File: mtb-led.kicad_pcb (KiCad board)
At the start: 2 copper layers, 120 x 50 mm, 60 parts, among them J7 AVR-ISP-6, J9 DEBUG, SW1 SW_Push, U1 ATmega328PB-A, U2 78M05, U3 TLC5940PWP, U4 TLC5940PWP, U5 MAX487E, Y1 14.7456 MHz

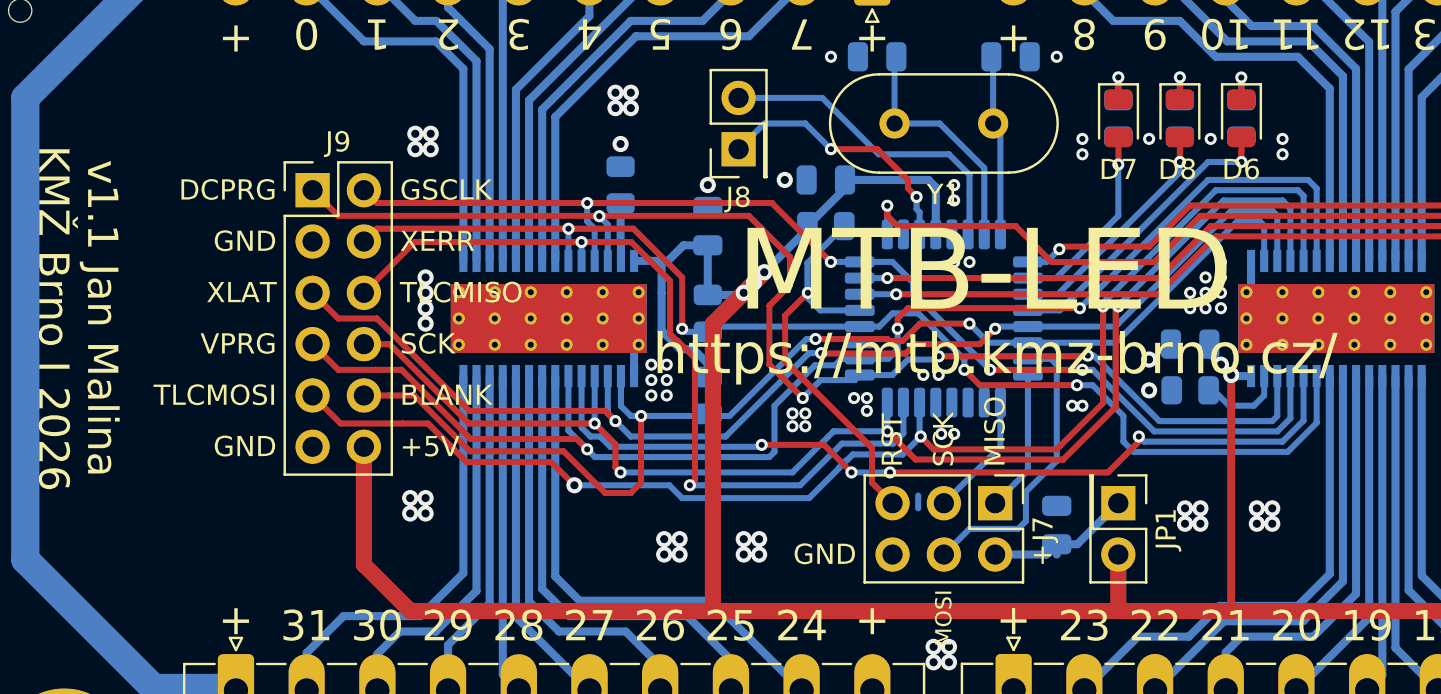
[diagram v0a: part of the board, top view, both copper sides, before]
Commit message: Remove XERR signal.
It is not used.
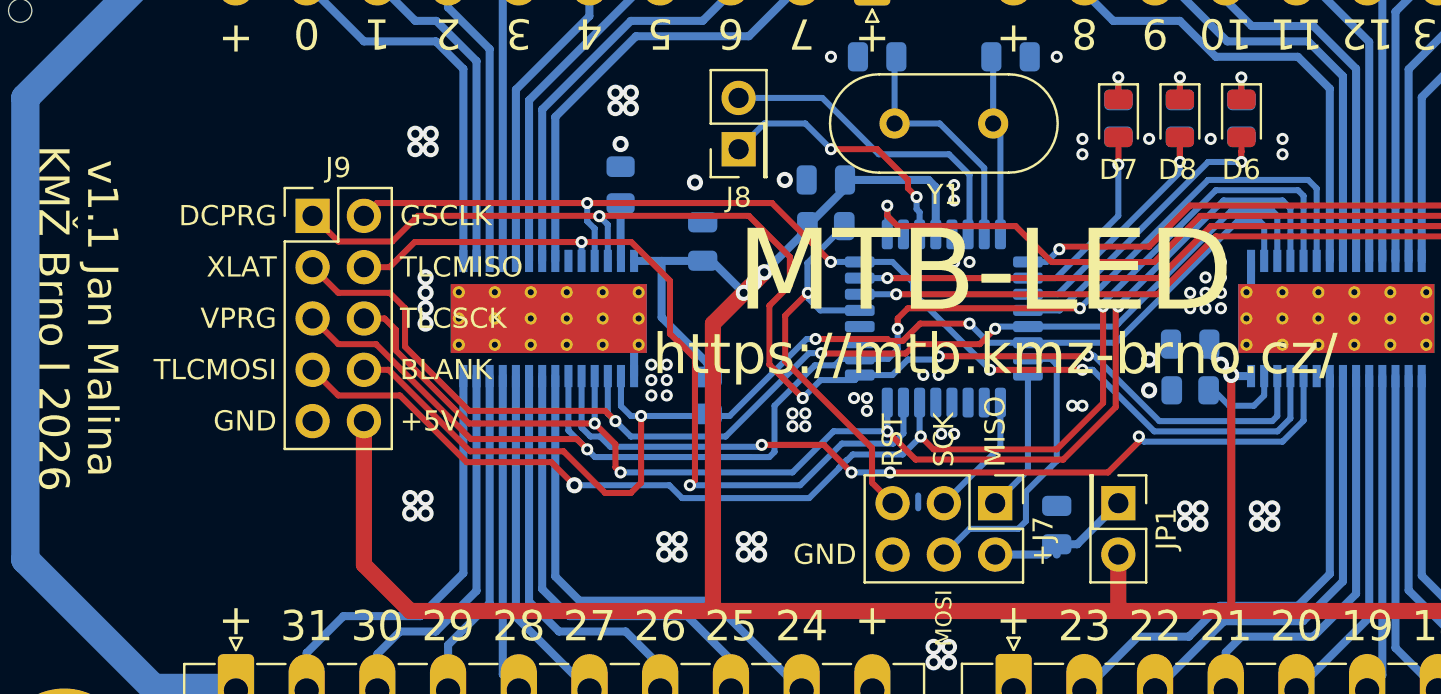
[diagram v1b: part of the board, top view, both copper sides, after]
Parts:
- removed R9: 10k, Resistor_SMD:R_0805_2012Metric
- J9: footprint Connector_PinHeader_2.54mm:PinHeader_2x06_P2.54mm_Vertical -> Connector_PinHeader_2.54mm:PinHeader_2x05_P2.54mm_Vertical
- moved J9 1.27 mm to (98.3, 89.4)
- moved C8 0.80 mm to (117.6, 90.7)
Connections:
- J9 pad 10: /BLANK -> +5V
- J9 pad 3: GND -> /XLAT
- J9 pad 4: /XERR -> /TLCMISO
- J9 pad 5: /XLAT -> /VPRG
- J9 pad 6: /TLCMISO -> /TLCSCK
- J9 pad 7: /VPRG -> /TLCMOSI
- J9 pad 8: /TLCSCK -> /BLANK
- J9 pad 9: /TLCMOSI -> GND
- U1 pad 28: /XERR -> unconnected-(U1-PC5-Pad28)
- U3 pad 23: /XERR -> unconnected-(U3-XERR-Pad23)
- U4 pad 23: /XERR -> unconnected-(U4-XERR-Pad23)
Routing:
- net /XERR: track 59.7 -> 0.00 mm, vias 4 -> 0
- net /XLAT: track 60.1 -> 61.7 mm
- net /TLCSCK: track 65.3 -> 66.4 mm
- net +5V: track 200.2 -> 199.1 mm
- net /VPRG: track 67.7 -> 68.2 mm
- net /TLCMISO: track 41.8 -> 41.3 mm
- net /TLCMOSI: track 66.0 -> 66.5 mm
- net /BLANK: track 59.5 -> 60.0 mm
- net /DCPRG: track 63.3 -> 63.8 mm
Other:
- board text added: "TLCSCK"
- board text removed: "XERR"

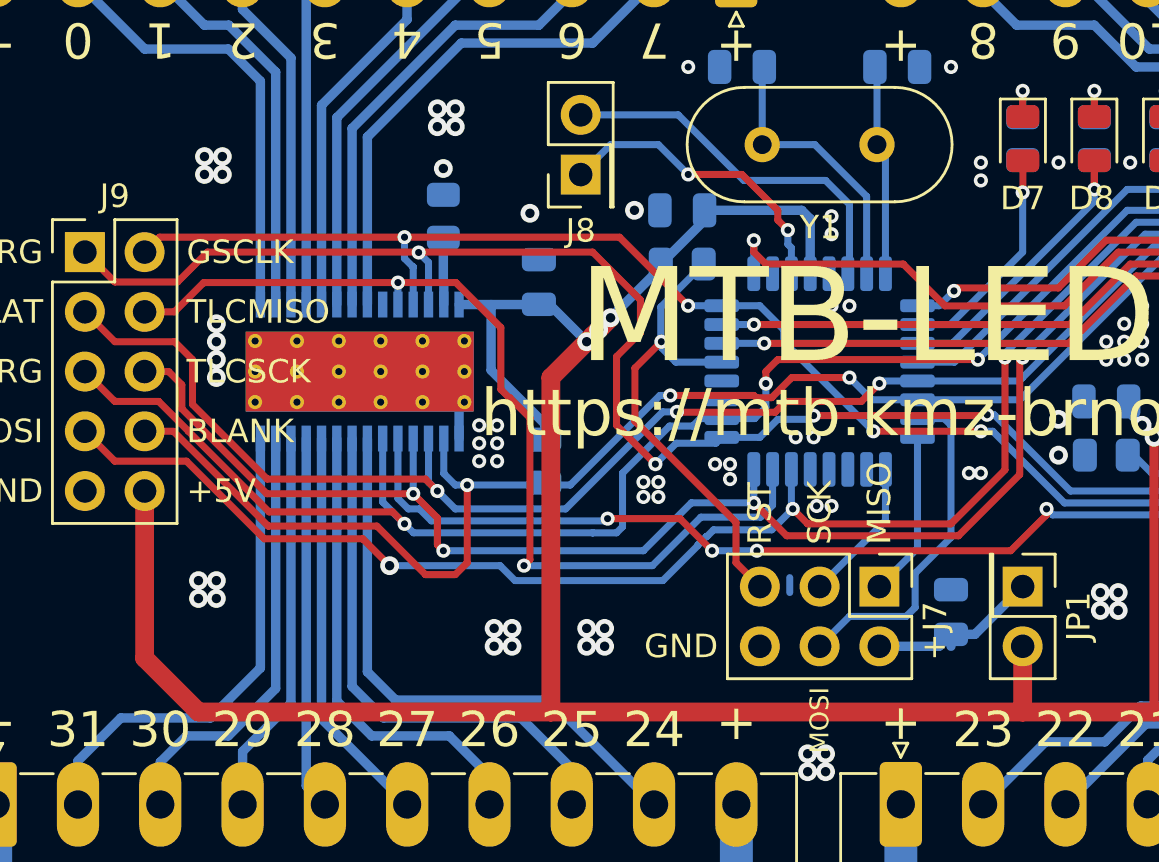
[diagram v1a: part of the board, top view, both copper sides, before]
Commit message: Add AREF 100nF capacitor.
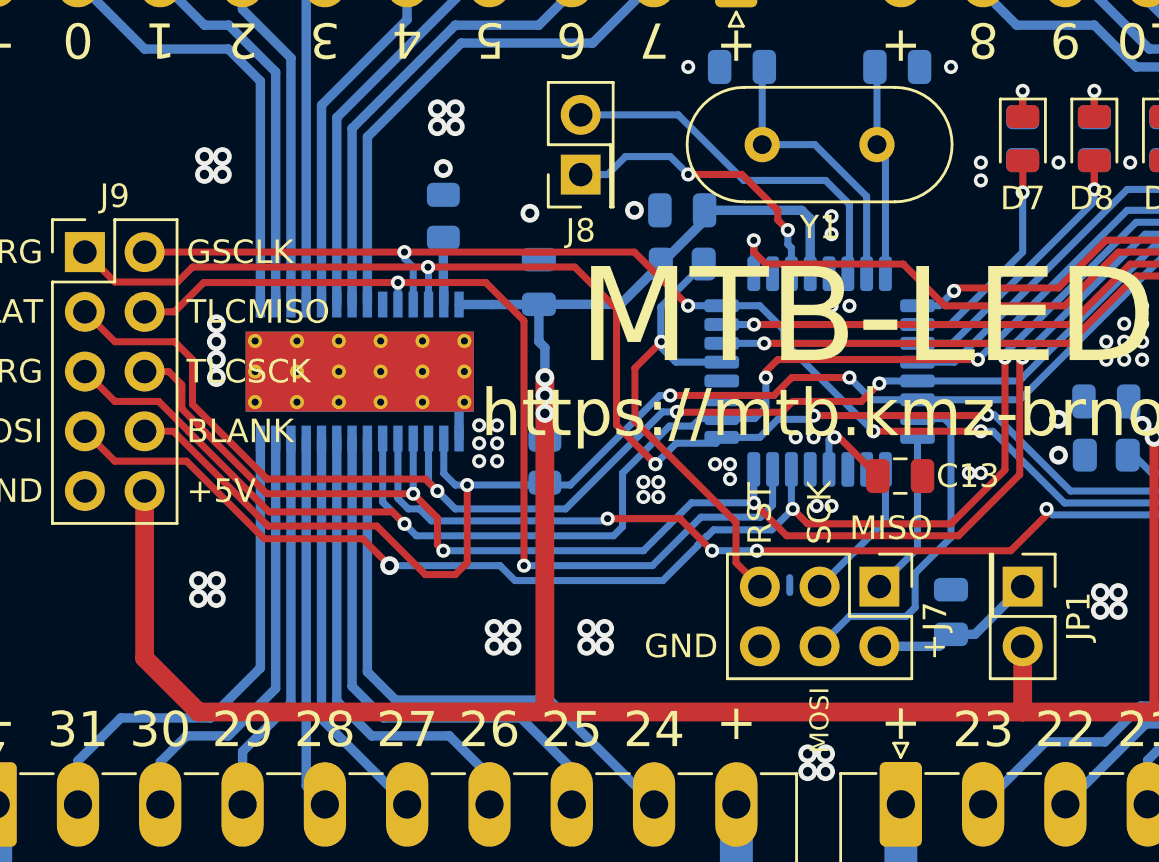
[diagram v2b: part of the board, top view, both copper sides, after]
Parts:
- added C13: 100n, Capacitor_SMD:C_0805_2012Metric, F.Cu at (133.0, 98.9)
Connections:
- U1 pad 20: unconnected-(U1-AREF-Pad20) -> Net-(U1-AREF)
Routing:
- net +5V: track 199.1 -> 193.7 mm
- net Net-(U1-AREF): track 0.00 -> 4.07 mm, vias 0 -> 1
- net /DCPRG: track 63.8 -> 60.8 mm
- net /GSCLK: track 56.5 -> 55.3 mm
- net /TLCMISO: track 41.3 -> 41.8 mm
- net Net-(J7-VCC): track 7.66 -> 7.15 mm

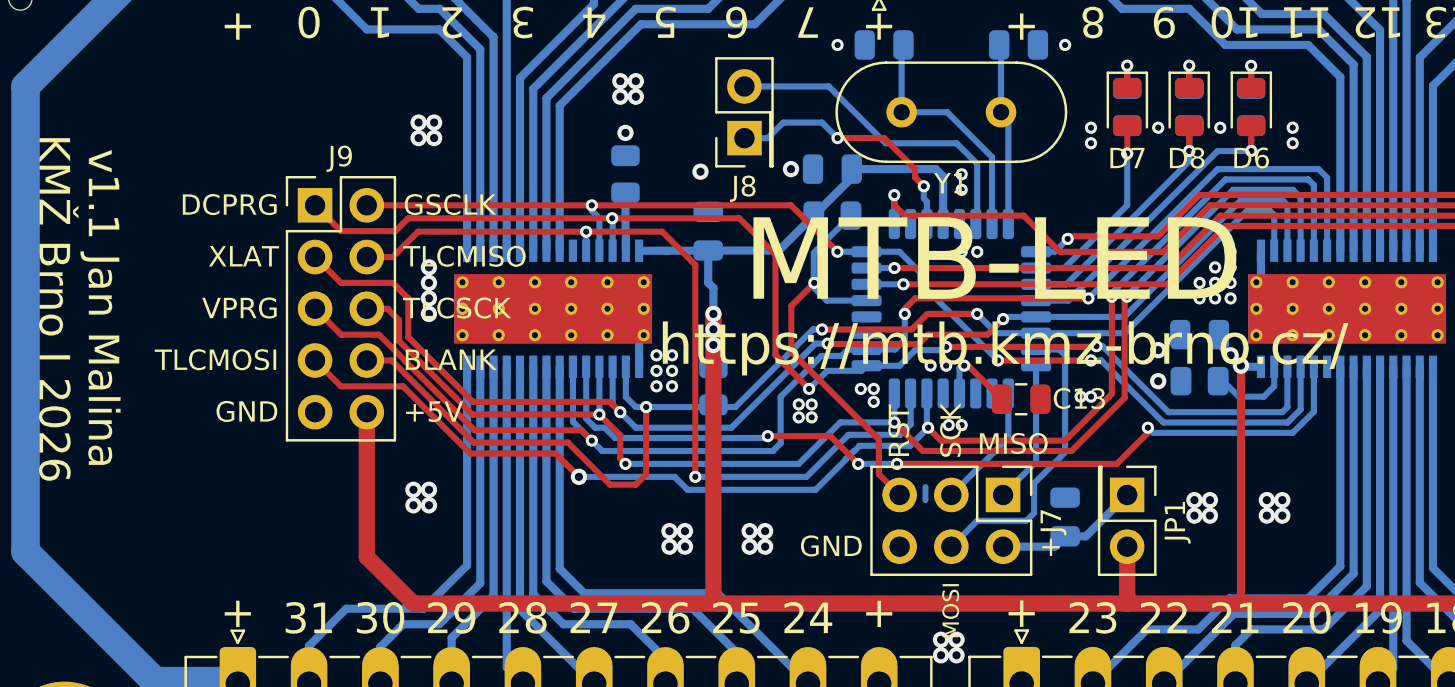
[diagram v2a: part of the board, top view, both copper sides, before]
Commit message: Remove DCPG & VPRG signals MCU <-> TLC.
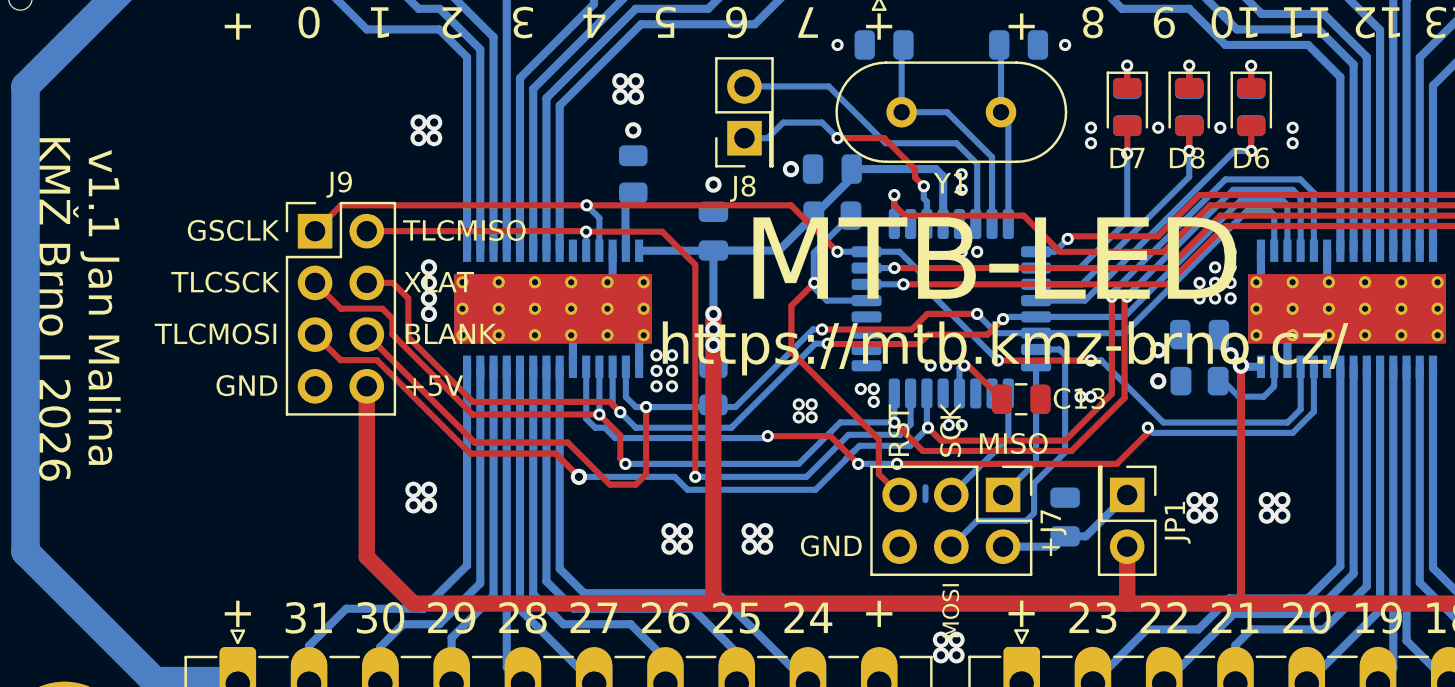
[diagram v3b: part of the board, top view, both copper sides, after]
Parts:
- J9: footprint Connector_PinHeader_2.54mm:PinHeader_2x05_P2.54mm_Vertical -> Connector_PinHeader_2.54mm:PinHeader_2x04_P2.54mm_Vertical
- moved J9 1.27 mm to (98.3, 90.7)
- moved R3 0.38 mm to (113.9, 87.9)
- moved C8 0.25 mm to (117.9, 90.7)
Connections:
- J9 pad 1: /DCPRG -> /GSCLK
- J9 pad 2: /GSCLK -> /TLCMISO
- J9 pad 3: /XLAT -> /TLCSCK
- J9 pad 4: /TLCMISO -> /XLAT
- J9 pad 5: /VPRG -> /TLCMOSI
- J9 pad 6: /TLCSCK -> /BLANK
- J9 pad 7: /TLCMOSI -> GND
- J9 pad 8: /BLANK -> +5V
- U1 pad 25: /DCPRG -> unconnected-(U1-PC2-Pad25)
- U1 pad 26: /VPRG -> unconnected-(U1-PC3-Pad26)
- U3 pad 26: /DCPRG -> GND
- U3 pad 6: /VPRG -> GND
- U4 pad 26: /DCPRG -> GND
- U4 pad 6: /VPRG -> GND
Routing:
- net /VPRG: track 68.3 -> 0.00 mm, vias 3 -> 0
- net /DCPRG: track 60.8 -> 0.00 mm, vias 4 -> 0
- net GND: track 3.92 -> 10.4 mm
- net /GSCLK: track 55.3 -> 58.5 mm
- net /XLAT: track 61.7 -> 58.7 mm
- net /TLCSCK: track 66.4 -> 69.3 mm
- net +5V: track 193.7 -> 195.1 mm
- net /BLANK: track 59.9 -> 60.4 mm
- net /TLCMISO: track 41.8 -> 41.3 mm
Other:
- board text removed: "DCPRG"
- board text removed: "VPRG"

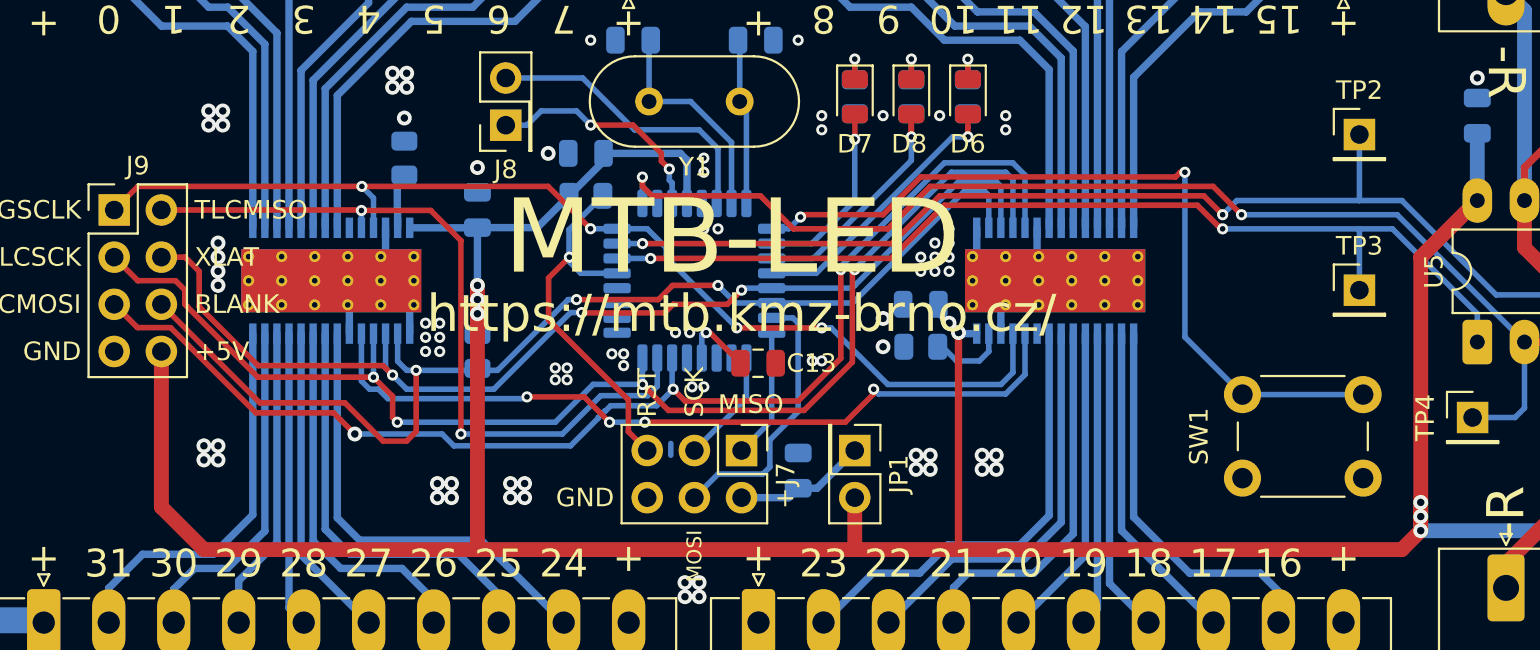
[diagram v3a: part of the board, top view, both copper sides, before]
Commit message: Fix ERC & DRC issues.
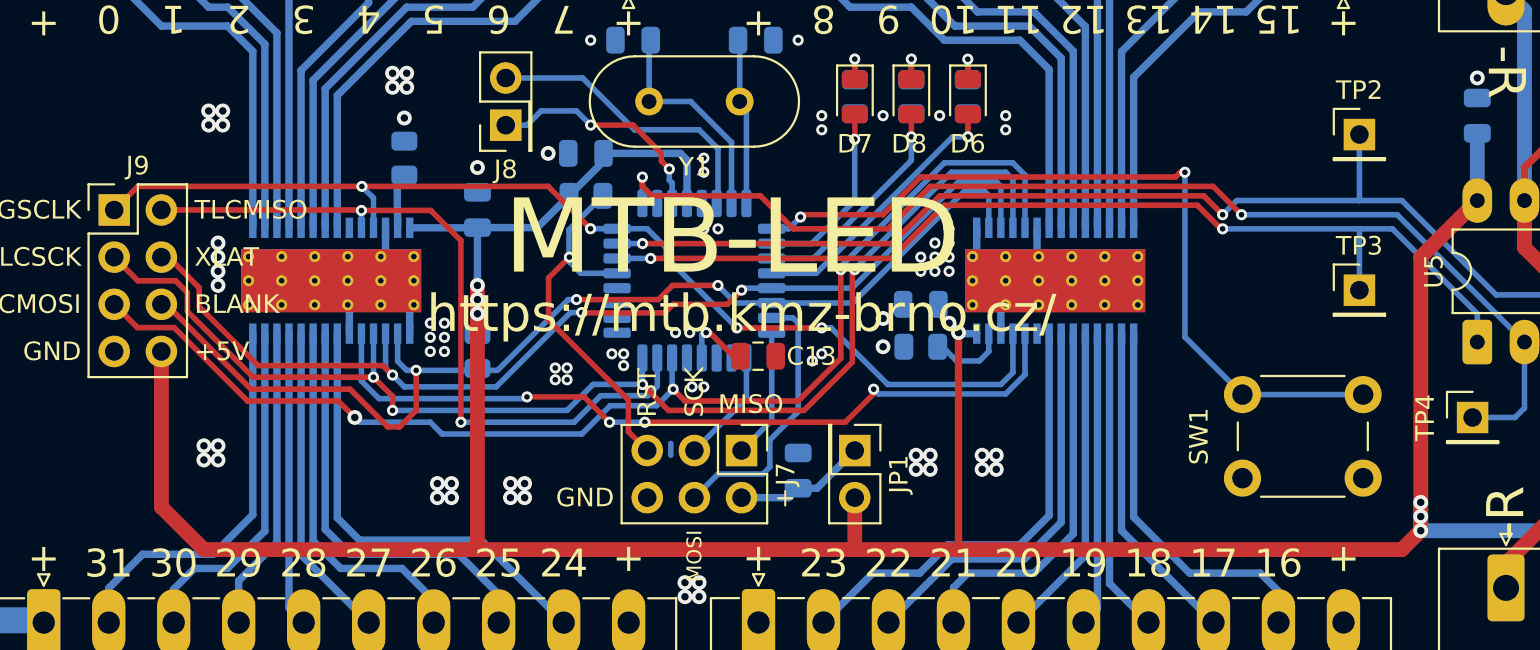
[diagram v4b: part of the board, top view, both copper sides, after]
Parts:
- moved C13 0.38 mm to (133.0, 98.6)
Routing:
- net /BLANK: track 60.4 -> 59.1 mm
- net /LED_RED: track 13.4 -> 12.2 mm
- net /TLCMISO: track 41.3 -> 40.4 mm
- net /XLAT: track 58.7 -> 58.1 mm
- net /TLCSCK: track 69.3 -> 68.7 mm
- net /TLCMOSI: track 66.8 -> 66.2 mm
